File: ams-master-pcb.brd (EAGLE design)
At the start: 203.2 x 101.6 mm, 246 parts, among them J1 M50-3601042, J2 TE-776087, J3 MUSBD11130, J4 MOLEX_43650-0416MOLEX_43650-0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, J6 MOLEX_43650-0416MOLEX_43650-0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, J7 43650-0616, Q1 STD45P4LLF6AG, Q2 BSS138, Q3 BSS138, Q4 BSS138, Q5 BSS138, Q6 BSS138, Q7 FQD3P50, Q8 FQD3P50, U1 PDS1-S5-S5-M-TR, U10 ISO7221, U11 ISO7221, U13 MCP2562FD, U14 SN74LVC541A, U16 LM3671MF-3.3/NOPB, U17 SN74LVC1G02DBV, U18 LM3671MF-1.2/NOPB, U2 SN74LVC1G32DBV, U22 FAN3214, U23 FAN3214, U24 CSD17506Q5A, U25 CSD17506Q5A, U27 CSD17506Q5A, U3 SN74LVC1G08DBV, U30 ISO7221, U31 ISO7221, U32 PDS1-S5-S5-M-TR, U33 ISO7221, U34 ISO7221, U35 PDS1-S5-S5-M-TR, U36 ADC121S021, U37 ADC121S021, U38 FT232RL, U42 TPS54540DDARQ1, U5 CD4050BD, U6 CD4050BD, U7 MCP2562FD, U8 ADUM3160BRWZ-RL, Y2 16MHz

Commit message: moving decoupling caps
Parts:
- moved C79 318.6 mm to (189.9, 57.1)
- moved C75 295.6 mm to (181.6, 58.4), turned to 90 degrees
- moved C76 290.1 mm to (175.9, 58.4), turned to 90 degrees
- moved C78 282.1 mm to (158.1, 47.6), turned to 90 degrees
- moved C80 274.9 mm to (139.7, 46.4)
- moved C77 271.9 mm to (152.4, 47.6), turned to 90 degrees
- moved C14 249.8 mm to (122.6, 38.1)
- moved C16 236.2 mm to (123.2, 34.3)
- moved C15 232.2 mm to (123.2, 36.2)
- moved C56 174.7 mm to (64.1, 90.8), turned to 270 degrees
- moved C11 169.0 mm to (34.3, 106.7)
- moved C12 159.9 mm to (34.3, 108.6)
- moved C6 158.3 mm to (21.0, 26.0)
- moved C7 151.6 mm to (21.0, 24.1)
- moved C10 147.1 mm to (28.3, 87.6), turned to 270 degrees
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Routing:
- net CURRENT_SENSE_-75_TO_75A: track 1.45 -> 52.2 mm
- net CURRENT_SENSE_-750_TO_750A: track 0.09 -> 50.5 mm
- net +3V3: track 100.7 -> 119.1 mm, vias 35 -> 40
- net GND: track 123.6 -> 137.6 mm, vias 104 -> 111
- net N$27: track 0.00 -> 4.95 mm
- net USB_D_N: track 4.50 -> 8.31 mm
- net USB_D_P: track 4.43 -> 8.24 mm
- net UART_RX: track 55.5 -> 51.7 mm
- net +5V: track 53.7 -> 54.5 mm
- net +5V/2: vias 5 -> 8

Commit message: DRC time
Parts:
- moved C12 22.8 mm to (29.2, 86.4), turned to 270 degrees
- moved C14 22.8 mm to (101.6, 29.2)
- moved C11 20.7 mm to (30.5, 86.4), turned to 270 degrees
- moved C16 11.9 mm to (112.4, 29.2), turned to 180 degrees
- moved C13 10.2 mm to (43.8, 85.7), turned to 90 degrees
- moved C9 4.02 mm to (10.8, 85.1), flipped to the bottom, turned to 270 degrees
- moved C10 3.62 mm to (31.8, 88.6), turned to 180 degrees
- moved R9 3.24 mm to (10.8, 88.9), flipped to the bottom, turned to 90 degrees
- moved C15 3.24 mm to (122.6, 33.0)
- moved U38 3.18 mm to (38.1, 87.0)
- moved R10 3.17 mm to (10.2, 92.1), flipped to the bottom, turned to 180 degrees
- moved LED13 2.54 mm to (34.9, 97.2)
- moved LED2 2.54 mm to (40.6, 97.2)
- moved LED3 2.54 mm to (42.5, 97.2)
- moved LED5 2.54 mm to (36.8, 97.2)
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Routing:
- net +15V: track 51.7 -> 209.8 mm, vias 13 -> 14
- net VOLTAGE_MONITOR_SCLK: track 0.00 -> 157.5 mm, vias 0 -> 3
- net VOLTAGE_MONITOR_MISO: track 0.00 -> 148.1 mm, vias 0 -> 3
- net VEHICLE_VOLTAGE_MONITOR_CS: track 0.00 -> 128.1 mm, vias 0 -> 2
- net VEHICLE_VOLTAGE_IS_AVAILABLE: track 0.00 -> 109.1 mm, vias 0 -> 2
- net CURRENT_SHORT_3V3: track 63.8 -> 145.5 mm, vias 4 -> 5
- net BATTERY_VOLTAGE_IS_AVAILABLE: track 6.89 -> 74.5 mm
- net 5KW_3V3: track 120.8 -> 175.8 mm, vias 5 -> 6
- net GND: track 137.6 -> 156.1 mm, vias 111 -> 122
- net +3V3: track 119.1 -> 134.8 mm, vias 40 -> 43
- net N$28: track 0.00 -> 10.3 mm
- net +5V: track 54.5 -> 63.4 mm, vias 15 -> 17
- net USBISO_VCC: track 0.00 -> 7.82 mm
- net USBISO_GND: track 0.00 -> 5.34 mm, vias 0 -> 1
- net USBISO_D_P: track 0.00 -> 4.18 mm
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- added copper zone on layer 1, net USBISO_GND
- added copper zone on layer 16, net USBISO_GND

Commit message: DRC passed
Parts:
- moved C7 9.09 mm to (19.1, 33.0)
- moved C6 1.91 mm to (22.9, 26.0)
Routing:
- net GND: track 156.1 -> 164.6 mm, vias 122 -> 125
- net GND1: track 15.7 -> 21.4 mm, vias 9 -> 10
- net +5V: track 63.4 -> 69.0 mm
- net SW_5V2: track 0.00 -> 3.55 mm
- net SC_FROM_OUTSIDE_SENSE: track 49.4 -> 52.7 mm
- net +5V/2: track 73.5 -> 76.5 mm
- net +3V3: track 134.8 -> 137.5 mm
- net CURRENT_SHORT_3V3: track 145.5 -> 148.2 mm
- net +5V/1: track 24.0 -> 26.3 mm
- net MCU_RESET1: track 22.0 -> 23.9 mm
- net N$7: track 0.00 -> 1.27 mm
- net N$41: track 0.00 -> 1.27 mm
- net N$40: track 0.00 -> 1.27 mm
- net N$39: track 0.00 -> 1.27 mm
- net N$24: track 0.00 -> 1.27 mm
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- added copper zone on layer 1, net +5V/1
- removed copper zone on layer 1, net N$6

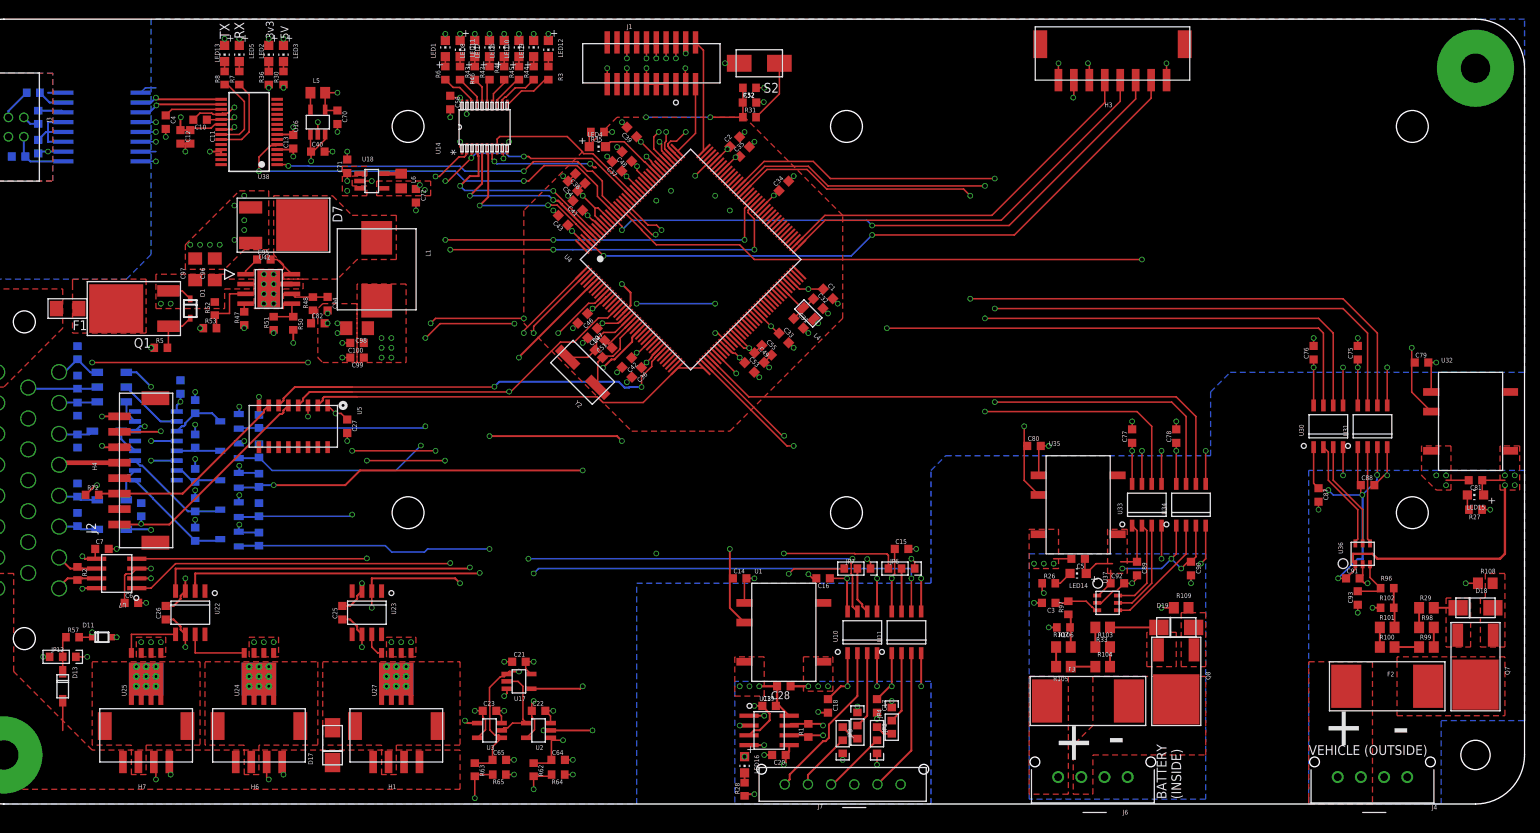
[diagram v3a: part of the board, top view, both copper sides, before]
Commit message: silkscreen done
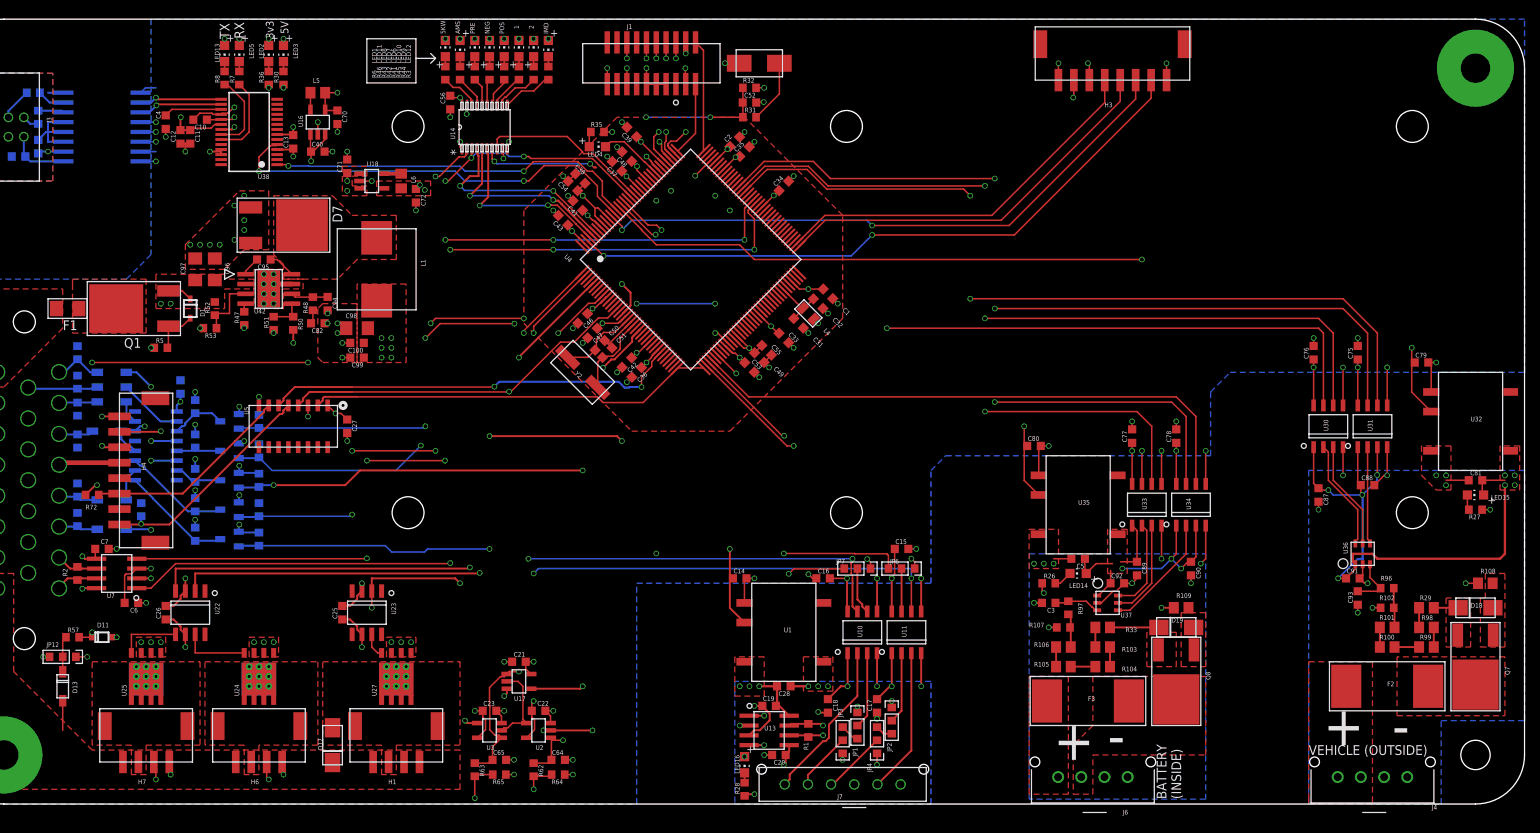
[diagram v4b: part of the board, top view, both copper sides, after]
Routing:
- net GND: track 164.6 -> 160.8 mm
- net +3V3: track 137.5 -> 136.2 mm
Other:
- board text added: "1"
- board text added: "2"
- board text added: "5KW"
- board text added: "AMS"
- board text added: "IMD"
- board text added: "NEG"
- board text added: "POS"
- board text added: "PRE"

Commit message: CAM processed
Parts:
- removed H3: 502443-0870, FormE:MOLEX_5024430870
- added JP5: (no value), pinhead:1X08/90
- moved U30 0.63 mm to (177.8, 49.5)
- moved U31 0.63 mm to (183.5, 49.5)
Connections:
- removed net INDICATOR_3: U4.124
- net +15V: now also JP5.8; no longer H3.1
- net +3V3: now also JP5.6; no longer H3.3
- net +5V: now also JP5.7; no longer H3.2
- net 5KW_3V3: now also JP5.3; no longer H3.6
- net CURRENT_SENSE_-750_TO_750A: now also JP5.5; no longer H3.4
- net CURRENT_SENSE_-75_TO_75A: now also JP5.4; no longer H3.5
- net CURRENT_SHORT_3V3: now also JP5.2; no longer H3.7
- net GND: now also JP5.1; no longer H3.8
- net INDICATOR_2: now also U4.124
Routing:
- net INDICATOR_2: track 15.4 -> 26.1 mm
- net +3V3: track 136.2 -> 130.9 mm, vias 43 -> 46
- net GND: track 160.8 -> 156.9 mm, vias 125 -> 124
- net +15V: track 209.8 -> 206.4 mm, vias 14 -> 13
- net CURRENT_SHORT_3V3: track 148.2 -> 151.2 mm
- net 5KW_3V3: track 175.8 -> 178.7 mm
- net CURRENT_SENSE_-75_TO_75A: track 52.1 -> 54.5 mm
- net +5V: track 69.0 -> 66.7 mm, vias 17 -> 16
- net CURRENT_SENSE_-750_TO_750A: track 50.5 -> 52.5 mm
- net +5V/2: track 76.5 -> 78.4 mm
- net GND2: track 21.5 -> 22.7 mm
- net POSITIVE_CONTACTOR_CTRL: track 111.7 -> 110.7 mm
- net +5V/3: track 37.7 -> 36.8 mm
- net VEHICLE_VOLTAGE_MONITOR_CS: track 128.1 -> 127.4 mm
- net NEGATIVE_CONTACTOR_CTRL: track 121.1 -> 120.4 mm
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- added copper zone on layer 1, net +3V3
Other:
- outline, holes or cut-outs redrawn
- board text added: "CONTACTOR NEG"
- board text added: "CONTACTOR POS"
- board text added: "CONTACTOR PRE"
- board text added: "FE07 AMS MASTER V1.0"
- board text added: "GLV"
- board text added: "GLV System"
- board text added: "HIGH VOLTAGE"
- board text added: "Missouri S&T Formula Electric"
